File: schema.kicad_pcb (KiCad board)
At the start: 2 copper layers, 43.7 x 40.5 mm, 7 parts, among them U1 74HC595D, U2 74HC595D, U5 AT28C256-15PU

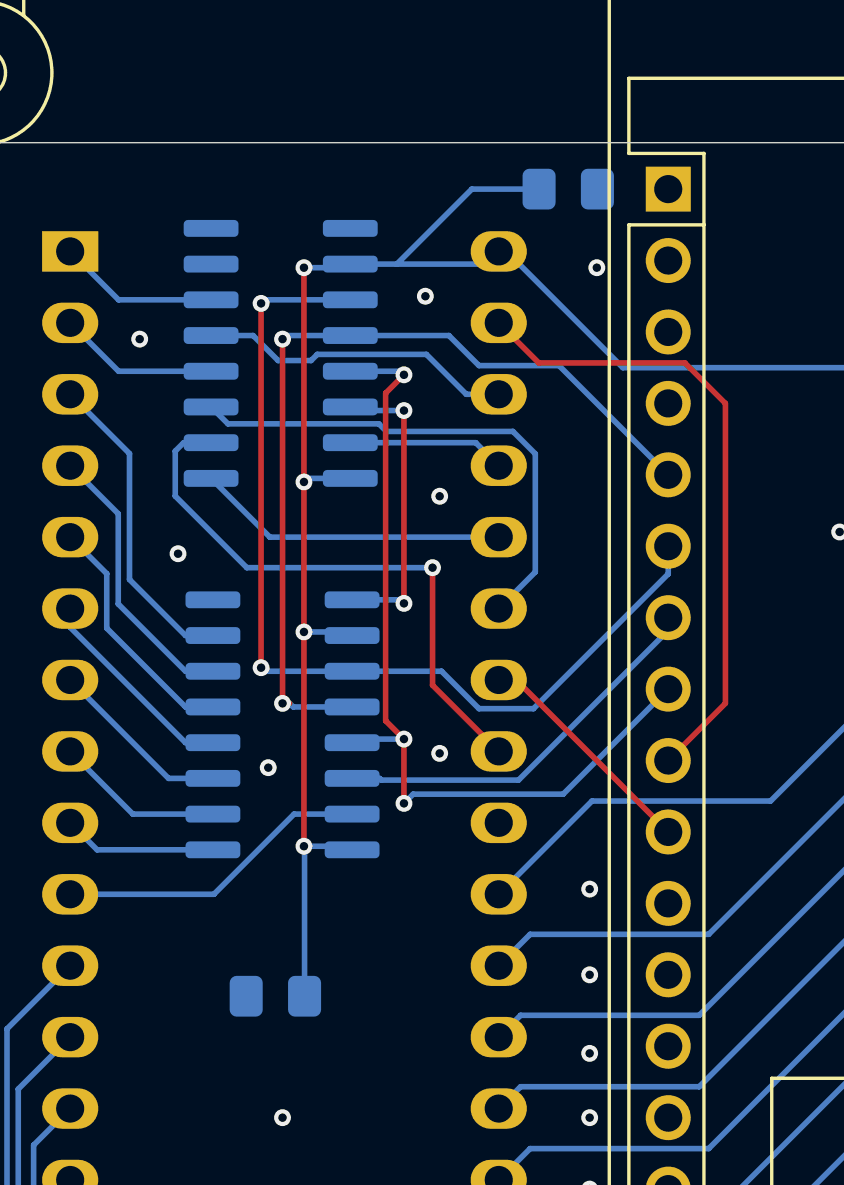
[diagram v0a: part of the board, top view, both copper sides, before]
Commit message: update condensators
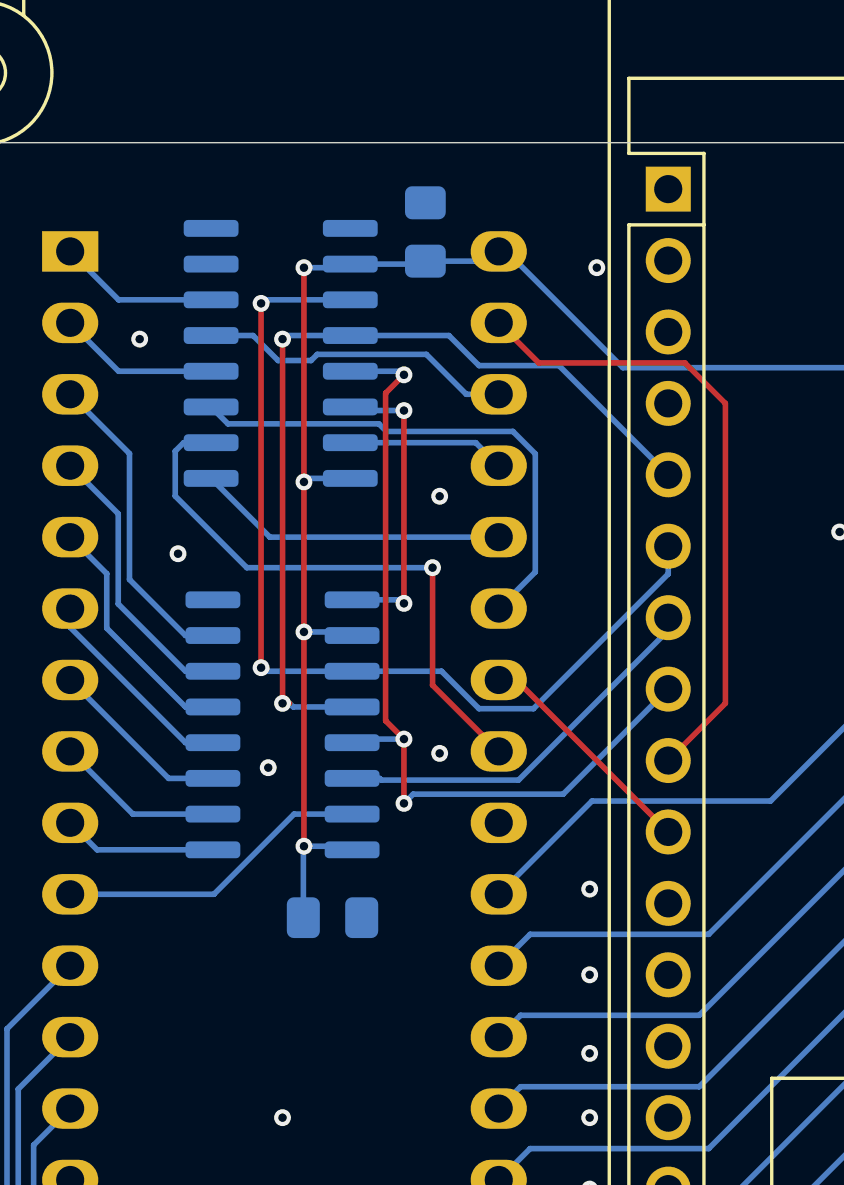
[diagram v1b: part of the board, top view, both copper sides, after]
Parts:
- C1, C2: value 100nC -> 100uC
- moved C1 5.30 mm to (138.2, 84.3), turned to 90 degrees
- moved C3 3.45 mm to (134.9, 108.7), turned to 0 degrees
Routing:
- net +5VD: track 71.1 -> 62.6 mm
- net GNDD: vias 15 -> 14
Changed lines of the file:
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@@
         (effects (font (size 1 1) (thickness 0.15)) (justify mirror))
     )
-    (fp_text value "100nC" (at 0 -1.68) (layer "B.Fab")
+    (fp_text value "100uC" (at 0 -1.68) (layer "B.Fab")
         (effects (font (size 1 1) (thickness 0.15)) (justify mirror))
     )
@@
   )
   (footprint "Capacitor_SMD:C_0805_2012Metric_Pad1.18x1.45mm_HandSolder" (layer "B.Cu")
-    (at 143.256 82.804)
+    (at 138.176 84.328 90)
     (descr "Capacitor SMD 0805 (2012 Metric), square (rectangular) end terminal, IPC_7351 nominal with elongated pad for handsoldering. (Body size source: IPC-SM-782 page 76, https://www.pcb-3d.com/wordpress/wp-content/uploads/ipc-sm-782a_amendment_1_and_2.pdf, https://docs.google.com/spreadsheets/d/1BsfQQcO9C6DZCsRaXUlFlo91Tg2WpOkGARC1WS5S8t0/edit?usp=sharing), generated with kicad-footprint-generator")
     (tags "capacitor handsolder")
@@
     (property "ki_keywords" "cap capacitor")
     (attr smd)
-    (fp_text reference "C1" (at 0 1.68) (layer "B.SilkS")
-        (effects (font (size 1 1) (thickness 0.15)) (justify mirror))
-    )
-    (fp_text value "100nC" (at 0 -1.68) (layer "B.Fab")
-        (effects (font (size 1 1) (thickness 0.15)) (justify mirror))
-    )
-    (fp_text user "${REFERENCE}" (at 0 0) (layer "B.Fab")
+    (fp_text reference "C1" (at 0 1.68 90) (layer "B.SilkS")
+        (effects (font (size 1 1) (thickness 0.15)) (justify mirror))
+    )
+    (fp_text value "100uC" (at 0 -1.68 90) (layer "B.Fab")
+        (effects (font (size 1 1) (thickness 0.15)) (justify mirror))
+    )
+    (fp_text user "${REFERENCE}" (at 0 0 90) (layer "B.Fab")
         (effects (font (size 0.5 0.5) (thickness 0.08)) (justify mirror))
     )
@@
     (fp_line (start 1 0.625) (end 1 -0.625)
       (stroke (width 0.1) (type solid)) (layer "B.Fab"))
-    (pad "1" smd roundrect (at -1.0375 0) (size 1.175 1.45) (layers "B.Cu" "B.Paste" "B.Mask") (roundrect_rratio 0.212766)
+    (pad "1" smd roundrect (at -1.0375 0 90) (size 1.175 1.45) (layers "B.Cu" "B.Paste" "B.Mask") (roundrect_rratio 0.212766)
       (net 47 "+5VD") (pintype "passive"))
-    (pad "2" smd roundrect (at 1.0375 0) (size 1.175 1.45) (layers "B.Cu" "B.Paste" "B.Mask") (roundrect_rratio 0.212766)
+    (pad "2" smd roundrect (at 1.0375 0 90) (size 1.175 1.45) (layers "B.Cu" "B.Paste" "B.Mask") (roundrect_rratio 0.212766)
       (net 4 "GNDD") (pintype "passive"))
     (model "${KICAD6_3DMODEL_DIR}/Capacitor_SMD.3dshapes/C_0805_2012Metric.wrl"
@@
   )
   (footprint "Capacitor_SMD:C_0805_2012Metric_Pad1.18x1.45mm_HandSolder" (layer "B.Cu")
-    (at 132.842 111.506 180)
+    (at 134.874 108.712)
     (descr "Capacitor SMD 0805 (2012 Metric), square (rectangular) end terminal, IPC_7351 nominal with elongated pad for handsoldering. (Body size source: IPC-SM-782 page 76, https://www.pcb-3d.com/wordpress/wp-content/uploads/ipc-sm-782a_amendment_1_and_2.pdf, https://docs.google.com/spreadsheets/d/1BsfQQcO9C6DZCsRaXUlFlo91Tg2WpOkGARC1WS5S8t0/edit?usp=sharing), generated with kicad-footprint-generator")
     (tags "capacitor handsolder")
@@
     (fp_line (start 1 0.625) (end 1 -0.625)
       (stroke (width 0.1) (type solid)) (layer "B.Fab"))
-    (pad "1" smd roundrect (at -1.0375 0 180) (size 1.175 1.45) (layers "B.Cu" "B.Paste" "B.Mask") (roundrect_rratio 0.212766)
+    (pad "1" smd roundrect (at -1.0375 0) (size 1.175 1.45) (layers "B.Cu" "B.Paste" "B.Mask") (roundrect_rratio 0.212766)
       (net 47 "+5VD") (pintype "passive"))
-    (pad "2" smd roundrect (at 1.0375 0 180) (size 1.175 1.45) (layers "B.Cu" "B.Paste" "B.Mask") (roundrect_rratio 0.212766)
+    (pad "2" smd roundrect (at 1.0375 0) (size 1.175 1.45) (layers "B.Cu" "B.Paste" "B.Mask") (roundrect_rratio 0.212766)
       (net 4 "GNDD") (pintype "passive"))
     (model "${KICAD6_3DMODEL_DIR}/Capacitor_SMD.3dshapes/C_0805_2012Metric.wrl"
@@
   (via (at 144.018 115.824) (size 0.6) (drill 0.3) (layers "F.Cu" "B.Cu") (free) (net 4))
   (via (at 138.684 102.87) (size 0.6) (drill 0.3) (layers "F.Cu" "B.Cu") (free) (net 4))
-  (via (at 138.176 86.614) (size 0.6) (drill 0.3) (layers "F.Cu" "B.Cu") (free) (net 4))
   (via (at 153.67 85.598) (size 0.6) (drill 0.3) (layers "F.Cu" "B.Cu") (free) (net 4))
   (via (at 129.380315 95.76949) (size 0.6) (drill 0.3) (layers "F.Cu" "B.Cu") (free) (net 4))
@@
   (via (at 133.858 106.172) (size 0.6) (drill 0.3) (layers "F.Cu" "B.Cu") (net 47))
   (segment (start 141.065 85.02) (end 145.199 89.154) (width 0.2) (layer "B.Cu") (net 47))
+  (segment (start 133.8365 108.712) (end 133.8365 106.1935) (width 0.2) (layer "B.Cu") (net 47))
+  (segment (start 140.4395 85.3655) (end 140.785 85.02) (width 0.2) (layer "B.Cu") (net 47))
   (segment (start 145.199 89.154) (end 160.782 89.154) (width 0.2) (layer "B.Cu") (net 47))
+  (segment (start 138.176 85.3655) (end 140.4395 85.3655) (width 0.2) (layer "B.Cu") (net 47))
   (segment (start 135.379 85.598) (end 135.506 85.471) (width 0.2) (layer "B.Cu") (net 47))
   (segment (start 133.858 98.552) (end 135.444 98.552) (width 0.2) (layer "B.Cu") (net 47))
-  (segment (start 139.827 82.804) (end 137.16 85.471) (width 0.2) (layer "B.Cu") (net 47))
   (segment (start 133.858 85.598) (end 135.379 85.598) (width 0.2) (layer "B.Cu") (net 47))
   (segment (start 135.506 93.091) (end 133.985 93.091) (width 0.2) (layer "B.Cu") (net 47))
   (segment (start 133.858 106.172) (end 135.444 106.172) (width 0.2) (layer "B.Cu") (net 47))
+  (segment (start 133.8365 106.1935) (end 133.858 106.172) (width 0.2) (layer "B.Cu") (net 47))
   (segment (start 133.8795 106.1935) (end 133.858 106.172) (width 0.2) (layer "B.Cu") (net 47))
   (segment (start 160.782 89.154) (end 162.052 90.424) (width 0.2) (layer "B.Cu") (net 47))
   (segment (start 135.444 98.552) (end 135.571 98.679) (width 0.2) (layer "B.Cu") (net 47))
-  (segment (start 135.506 85.471) (end 137.16 85.471) (width 0.2) (layer "B.Cu") (net 47))
   (segment (start 133.985 93.091) (end 133.858 93.218) (width 0.2) (layer "B.Cu") (net 47))
+  (segment (start 138.0705 85.471) (end 138.176 85.3655) (width 0.2) (layer "B.Cu") (net 47))
   (segment (start 135.444 106.172) (end 135.571 106.299) (width 0.2) (layer "B.Cu") (net 47))
-  (segment (start 133.8795 111.506) (end 133.8795 106.1935) (width 0.2) (layer "B.Cu") (net 47))
+  (segment (start 135.506 85.471) (end 138.0705 85.471) (width 0.2) (layer "B.Cu") (net 47))
   (segment (start 140.785 85.02) (end 141.065 85.02) (width 0.2) (layer "B.Cu") (net 47))
-  (segment (start 137.16 85.471) (end 140.334 85.471) (width 0.2) (layer "B.Cu") (net 47))
-  (segment (start 142.4725 82.804) (end 139.827 82.804) (width 0.2) (layer "B.Cu") (net 47))
   (segment (start 140.334 85.471) (end 140.785 85.02) (width 0.2) (layer "B.Cu") (net 47))
   (segment (start 161.798 90.678) (end 162.052 90.424) (width 0.2) (layer "B.Cu") (net 47))

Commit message: update capacitor to 10uC
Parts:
- C1: value 100uC -> 10uC
- C2: value 100uC -> 100nC
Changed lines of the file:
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@@
         (effects (font (size 1 1) (thickness 0.15)) (justify mirror))
     )
-    (fp_text value "100uC" (at 0 -1.68) (layer "B.Fab")
+    (fp_text value "100nC" (at 0 -1.68) (layer "B.Fab")
         (effects (font (size 1 1) (thickness 0.15)) (justify mirror))
     )
@@
         (effects (font (size 1 1) (thickness 0.15)) (justify mirror))
     )
-    (fp_text value "100uC" (at 0 -1.68 90) (layer "B.Fab")
+    (fp_text value "10uC" (at 0 -1.68 90) (layer "B.Fab")
         (effects (font (size 1 1) (thickness 0.15)) (justify mirror))
     )

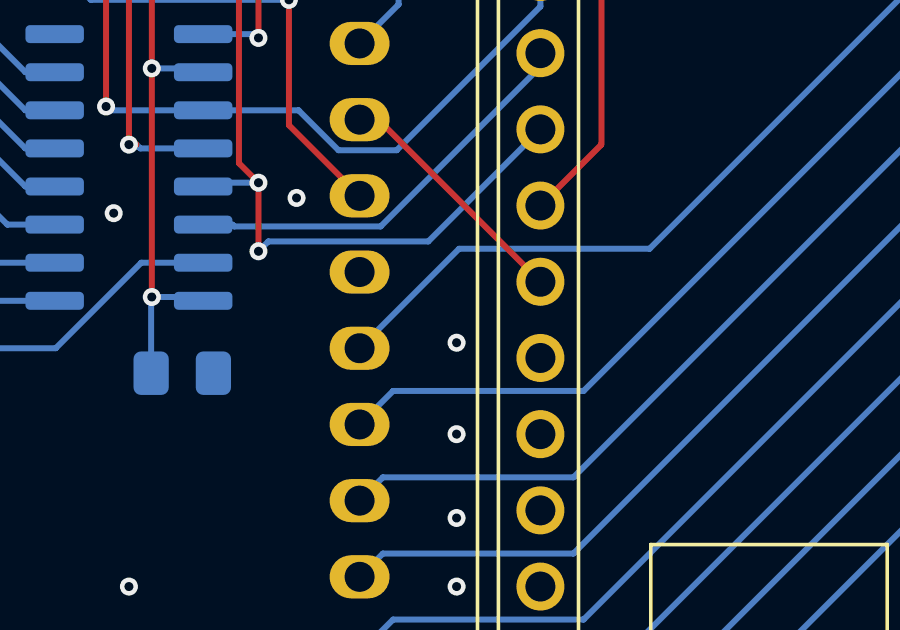
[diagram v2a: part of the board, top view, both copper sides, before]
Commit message: reroute eeprom cs to arduino
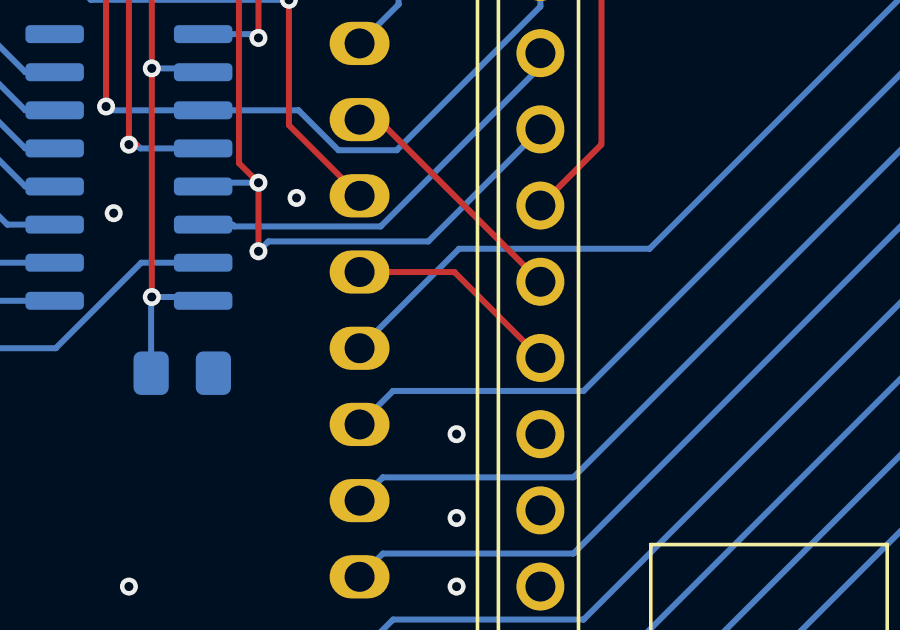
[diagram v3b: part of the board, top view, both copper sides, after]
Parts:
- C3: value 100nC -> 10uC
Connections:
- A1 pad 11: unconnected-(A1-D8-Pad11) -> Net-(A1-D8)
- U5 pad 20: GNDD -> Net-(A1-D8)
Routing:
- net Net-(A1-D8): track 0.00 -> 7.21 mm
- net GNDD: vias 14 -> 13
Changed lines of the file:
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@@
   (net 9 "Net-(A1-D6)")
   (net 10 "Net-(A1-D7)")
-  (net 11 "unconnected-(A1-D8-Pad11)")
+  (net 11 "Net-(A1-D8)")
   (net 12 "unconnected-(A1-D9-Pad12)")
   (net 13 "unconnected-(A1-D10-Pad13)")
@@
       (net 10 "Net-(A1-D7)") (pinfunction "D7") (pintype "bidirectional"))
     (pad "11" thru_hole oval (at 0 25.4) (size 1.6 1.6) (drill 1) (layers "*.Cu" "*.Mask")
-      (net 11 "unconnected-(A1-D8-Pad11)") (pinfunction "D8") (pintype "bidirectional"))
+      (net 11 "Net-(A1-D8)") (pinfunction "D8") (pintype "bidirectional"))
     (pad "12" thru_hole oval (at 0 27.94) (size 1.6 1.6) (drill 1) (layers "*.Cu" "*.Mask")
       (net 12 "unconnected-(A1-D9-Pad12)") (pinfunction "D9") (pintype "bidirectional"))
@@
       (net 26 "/D7") (pinfunction "D7") (pintype "tri_state"))
     (pad "20" thru_hole oval (at 15.24 20.32) (size 2 1.44) (drill 1) (layers "*.Cu" "*.Mask")
-      (net 4 "GNDD") (pinfunction "~{CS}") (pintype "input"))
+      (net 11 "Net-(A1-D8)") (pinfunction "~{CS}") (pintype "input"))
     (pad "21" thru_hole oval (at 15.24 17.78) (size 2 1.44) (drill 1) (layers "*.Cu" "*.Mask")
       (net 39 "/A10") (pinfunction "A10") (pintype "input"))
@@
     (property "ki_keywords" "HCMOS SR 3State")
     (attr smd)
-    (fp_text reference "U1" (at 0 5.9) (layer "B.SilkS")
+    (fp_text reference "U1" (at -1.27 5.9) (layer "B.SilkS")
         (effects (font (size 1 1) (thickness 0.15)) (justify mirror))
     )
@@
     (property "ki_keywords" "cap capacitor")
     (attr smd)
-    (fp_text reference "C1" (at 0 1.68 90) (layer "B.SilkS")
+    (fp_text reference "C1" (at -2.794 0 180) (layer "B.SilkS")
         (effects (font (size 1 1) (thickness 0.15)) (justify mirror))
     )
@@
         (effects (font (size 1 1) (thickness 0.15)) (justify mirror))
     )
-    (fp_text value "100nC" (at 0 -1.68) (layer "B.Fab")
+    (fp_text value "10uC" (at 0 -1.68) (layer "B.Fab")
         (effects (font (size 1 1) (thickness 0.15)) (justify mirror))
     )
@@
   )
   (via (at 144.018 113.538) (size 0.6) (drill 0.3) (layers "F.Cu" "B.Cu") (free) (net 4))
-  (via (at 144.018 107.696) (size 0.6) (drill 0.3) (layers "F.Cu" "B.Cu") (free) (net 4))
   (via (at 144.018 118.364) (size 0.6) (drill 0.3) (layers "F.Cu" "B.Cu") (free) (net 4))
   (via (at 138.684 93.726) (size 0.6) (drill 0.3) (layers "F.Cu" "B.Cu") (free) (net 4))
@@
   (segment (start 141.408 100.26) (end 146.812 105.664) (width 0.2) (layer "F.Cu") (net 10))
   (segment (start 140.785 100.26) (end 141.408 100.26) (width 0.2) (layer "F.Cu") (net 10))
+  (segment (start 143.948 105.34) (end 146.812 108.204) (width 0.2) (layer "F.Cu") (net 11))
+  (segment (start 140.785 105.34) (end 143.948 105.34) (width 0.2) (layer "F.Cu") (net 11))
   (segment (start 152.532 120.264) (end 124.720628 120.264) (width 0.2) (layer "B.Cu") (net 19))
   (segment (start 123.298 118.841371) (end 123.298 112.667) (width 0.2) (layer "B.Cu") (net 19))
